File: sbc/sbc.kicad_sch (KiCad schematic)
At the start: 30 parts, among them SW1 RESET, SW2 NMI, U1 WD65C02, U2 ATF22V10C, U3 28C256, U4 AS7C256B, U5 DS1813, U6 MAX6816, X1 8MHz

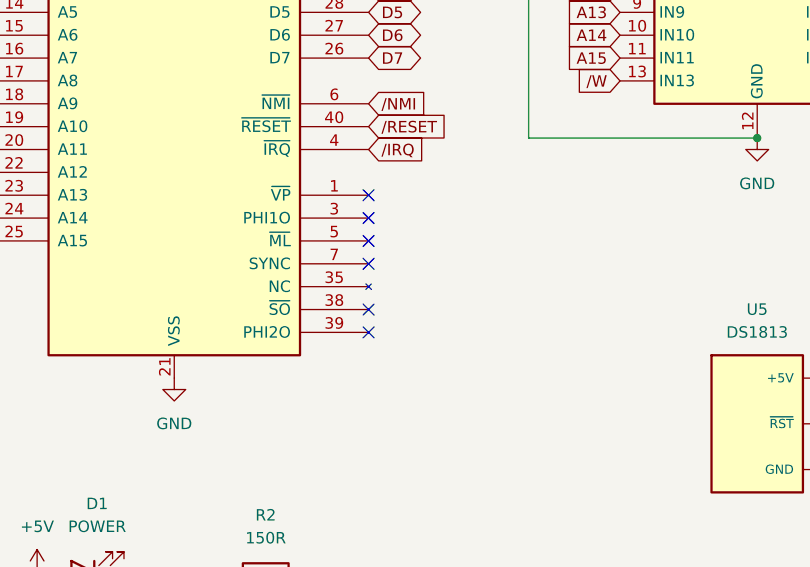
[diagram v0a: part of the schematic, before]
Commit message: SBC v2.3
Fixes over v2.2:

  - SBC: Fix the VIA footprint: CA1 and CB1 are inputs
  - SBC: Move the microSD power enable line from (VIA3) CA1 (input) to CA2 (output)
  - SBC: Tie 65C02 SOB high
  - Controller: connect LED enable
  - Controller: SMT switches
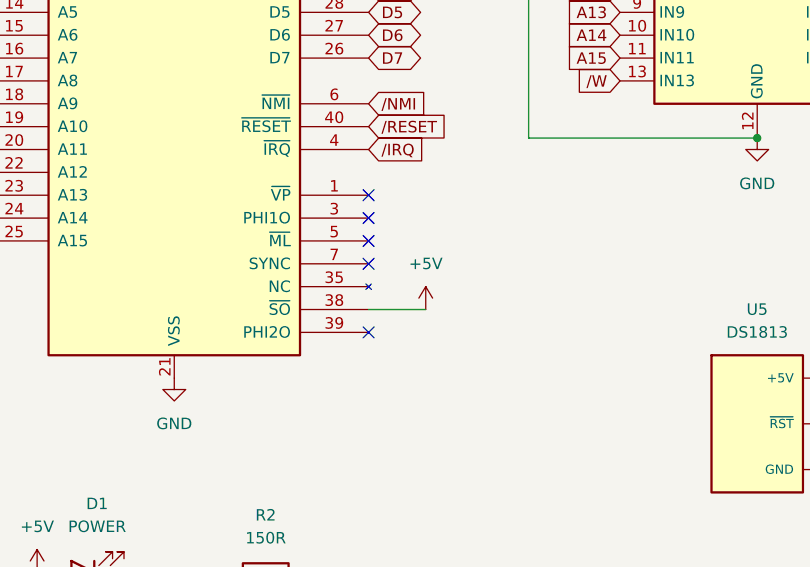
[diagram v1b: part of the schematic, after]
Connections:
- net +5V: now also U1.38 (~{SO})
- no-connect marks 8 -> 7
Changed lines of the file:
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@@
   (title_block
     (title "6502 SBC")
-    (date "2022-03-07")
-    (rev "2.2")
+    (date "2023-02-07")
+    (rev "2.3")
   )
   (junction (at 59.69 190.5) (diameter 0) (color 0 0 0 0)
@@
   (no_connect (at 81.28 82.55))
   (no_connect (at 81.28 85.09))
-  (no_connect (at 81.28 90.17))
   (no_connect (at 173.99 119.38))
   (wire (pts (xy 140.97 102.87) (xy 147.32 102.87))
@@
   )
   (wire (pts (xy 46.99 190.5) (xy 59.69 190.5))
+    (stroke (width 0) (type default) (color 0 0 0 0))
+  )
+  (wire (pts (xy 81.28 90.17) (xy 87.63 90.17))
     (stroke (width 0) (type default) (color 0 0 0 0))
   )
@@
     (pin "3")
   )
+  (symbol (lib_id "power:+5V") (at 87.63 90.17 0) (unit 1)
+    (in_bom yes) (on_board yes) (fields_autoplaced)
+    (property "Reference" "#PWR0145" (id 0) (at 87.63 93.98 0)
+      (effects (font (size 1.27 1.27)) hide)
+    )
+    (property "Value" "+5V" (id 1) (at 87.63 85.09 0))
+    (property "Footprint" "" (id 2) (at 87.63 90.17 0)
+      (effects (font (size 1.27 1.27)) hide)
+    )
+    (property "Datasheet" "" (id 3) (at 87.63 90.17 0)
+      (effects (font (size 1.27 1.27)) hide)
+    )
+    (pin "1")
+  )
   (symbol (lib_id "Device:C") (at 46.99 186.69 0) (unit 1)
     (in_bom yes) (on_board yes) (fields_autoplaced)
@@
       (reference "#PWR0144") (unit 1) (value "+3.3V") (footprint "")
     )
+    (path "/b9cf334a-4975-4133-9f18-324d40fb7d09"
+      (reference "#PWR0145") (unit 1) (value "+5V") (footprint "")
+    )
     (path "/005f7bba-a8a9-4e07-ad6d-de2e5146ff30/f30f7237-8b62-45bb-9411-6953bbc30ae0"
